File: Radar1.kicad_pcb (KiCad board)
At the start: 4 copper layers, 60 x 42 mm, 99 parts, among them J1 USB4215-03-A, J2 Barrel_Jack, J3 SMA-2.92mm-EndLaunch, J4 SMA-2.92mm-EndLaunch, U1 BGT24LTR11N16, U10 93LC56B-I/SN, U11 445I23D12M00000, U12 AMM-8211PSM, U13 TPS7A4700RGWT, U14 TPS7A2033PDBVR, U15 TPD2E009DBZR, U16 REF5025AID, U2 ADF4159WCCPZ, U3 OPA1656ID, U4 TPS7A2033PDBVR, U5 TPS7A2018PDBVR, U6 TPS7A4700RGWT, U7 FT2232HL-REEL, U8 ADS8353IPW, U9 ADP5600ACPZ-R7, Y1 ECS-TXO-2520MV-500-AN-TR

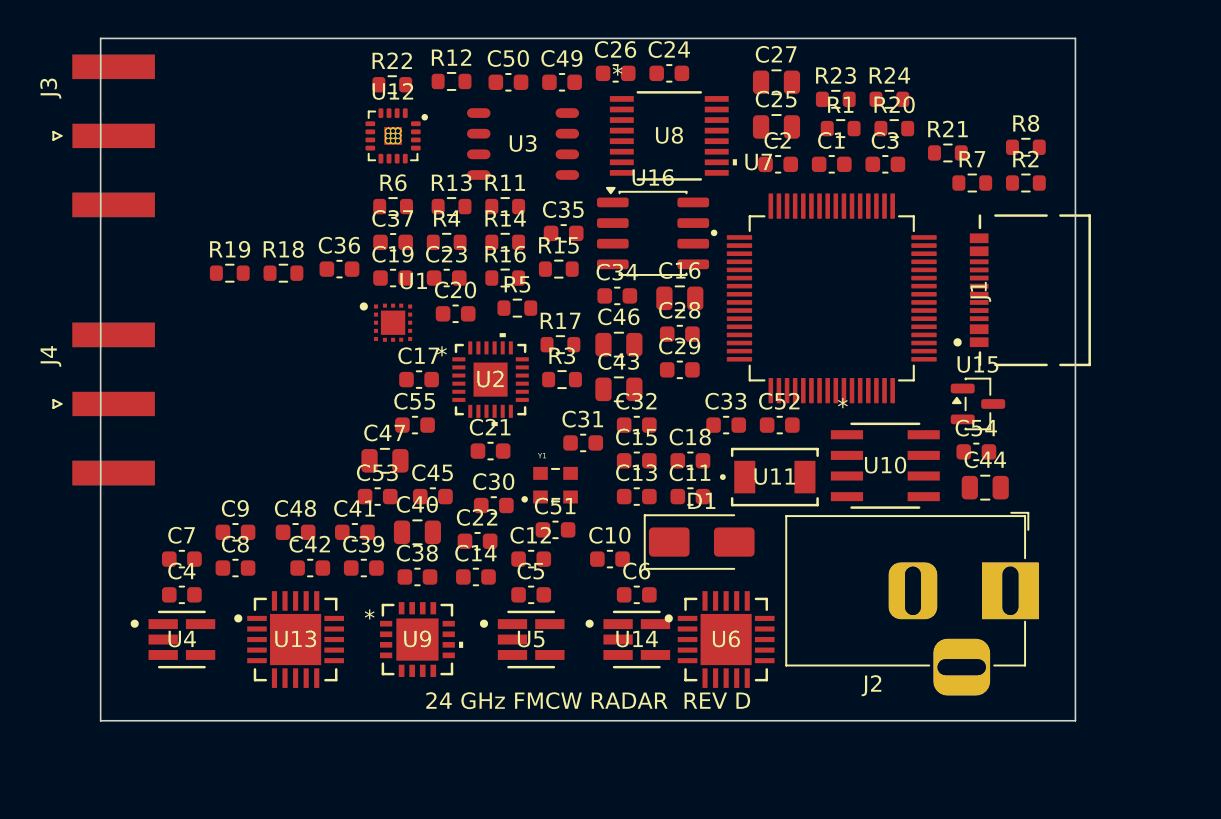
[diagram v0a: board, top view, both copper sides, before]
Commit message: RF routing: GCPW TX/RX lines, 4-layer GND/PWR zones, EP thermal vias
- tools/route_pcb.py (pcbnew API): F.Cu/In1/B.Cu GND zones + In2 +5V zone,
  EP thermal via arrays, 24 GHz GCPW (0.5 mm / 0.25 gap) with GND via fences
- Neck-down to pad width at QFN pad exits (0.5 mm line vs 0.5 mm-pitch pads)
- Via fence self-avoidance against RF copper; RF corridor keepouts in board_gen
  so auto-slotted passives stay out of the GCPW paths
- AMM-8211 footprint: EP thermal vias 9@0.3mm -> 4@0.6mm pitch (fab-safe webs)
- DRC: copper clean; remaining = 172 unconnected (signals, next phase),
  10 J3/J4 edge-launch waivers, silk cosmetics

Co-Authored-By: Claude Fable 5 <noreply@anthropic.com>
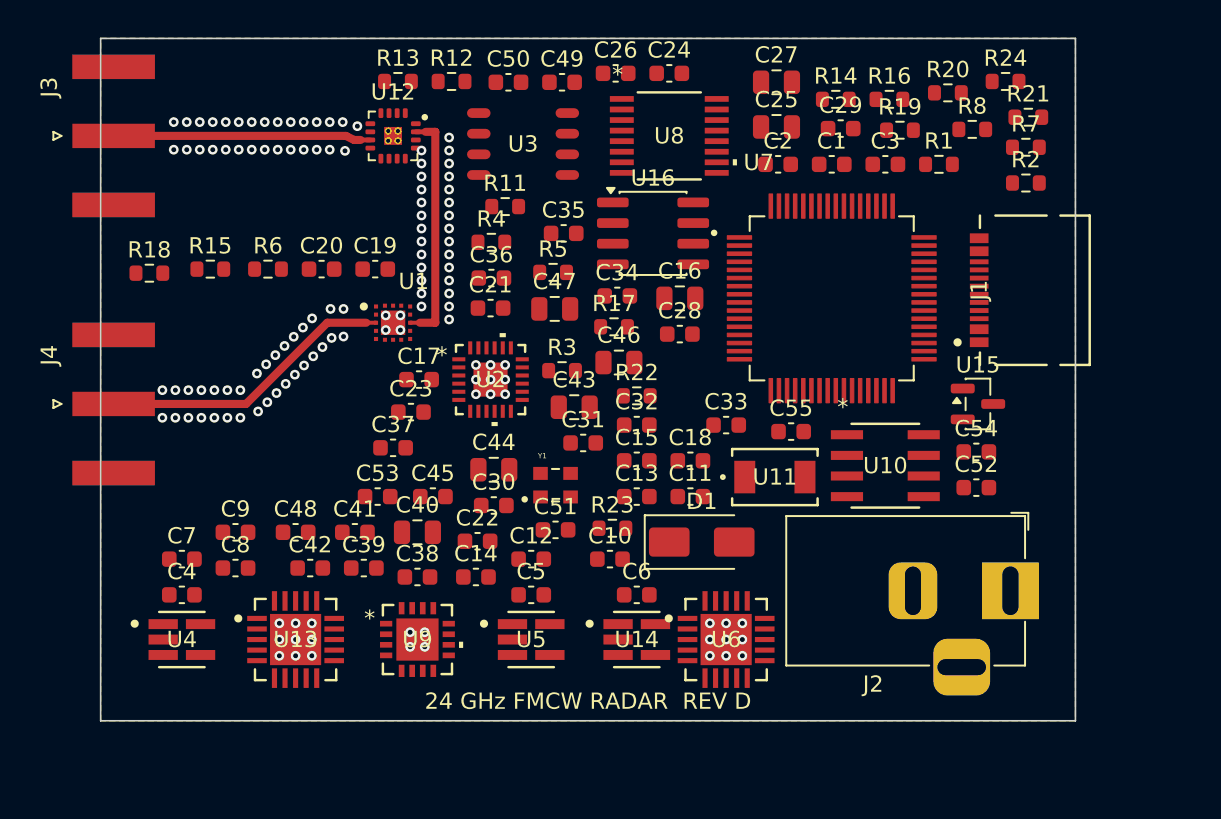
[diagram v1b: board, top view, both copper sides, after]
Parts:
- moved R19 42.2 mm to (109.2, 45.6)
- moved C44 30.3 mm to (84.2, 66.5)
- moved R23 29.8 mm to (91.5, 70.2)
- moved R16 26.1 mm to (108.5, 43.8)
- moved R22 24.4 mm to (93.0, 62.0)
- moved C55 23.2 mm to (102.5, 64.2)
- moved R14 22.2 mm to (105.2, 43.8)
- moved R15 21.5 mm to (66.8, 54.2)
- moved C29 17.8 mm to (105.5, 45.5)
- moved C47 14.0 mm to (88.0, 56.6)
- moved C52 12.7 mm to (113.9, 67.7)
- moved C37 12.7 mm to (78.0, 65.2)
- moved C36 9.37 mm to (84.0, 54.8)
- moved C21 8.80 mm to (84.0, 56.6)
- moved C20 8.70 mm to (73.6, 54.2)
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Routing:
- net ANT_RX: track 0.00 -> 18.2 mm
- net ANT_TX: track 0.00 -> 15.9 mm
- net RF_TX: track 0.00 -> 14.5 mm
- net GND: vias 0 -> 125
- added copper zone on In2.Cu, net +5V
- added copper zone on B.Cu, net GND
- added copper zone on F.Cu, net GND
- added copper zone on In1.Cu, net GND

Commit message: Phase C routing: A* signal/power router, In2 split planes, board 66x46
tools/route_signals.py: 0.2mm-grid A* over F.Cu/B.Cu with through-vias.
- escape stubs on fine-pitch ICs, escape-limited nets routed first
- In2 becomes a split plane: +3V3_RF west / +1V8 center / +3V3_DIG east
  over the +5V base fill; rail pads stitch down with vias, stragglers
  routed as tracks; GND stitching to In1 near every ground pad
- rip-up & reroute for sealed legs; geometric heal pass reconnects
  cluster splits from exact copper geometry
- board grown 60x42 -> 66x46 (placement was at ~95% usable density),
  edge connectors and south LDO row shifted with the edges
- board_gen: courtyard-based bboxes, RF-pocket ownership guard, IC
  routing halos, U2/U7 bus-lane keepouts, stair-stepped ANT_RX keepout

DRC: 172 -> 28 unconnected items (19 net splits remain, all in the RF
pocket / U2-east / U7-west / J1 congestion spots); zero clearance or
short errors; 10 J3/J4 edge-launch waivers as before. Renders in docs/.

Co-Authored-By: Claude Fable 5 <noreply@anthropic.com>
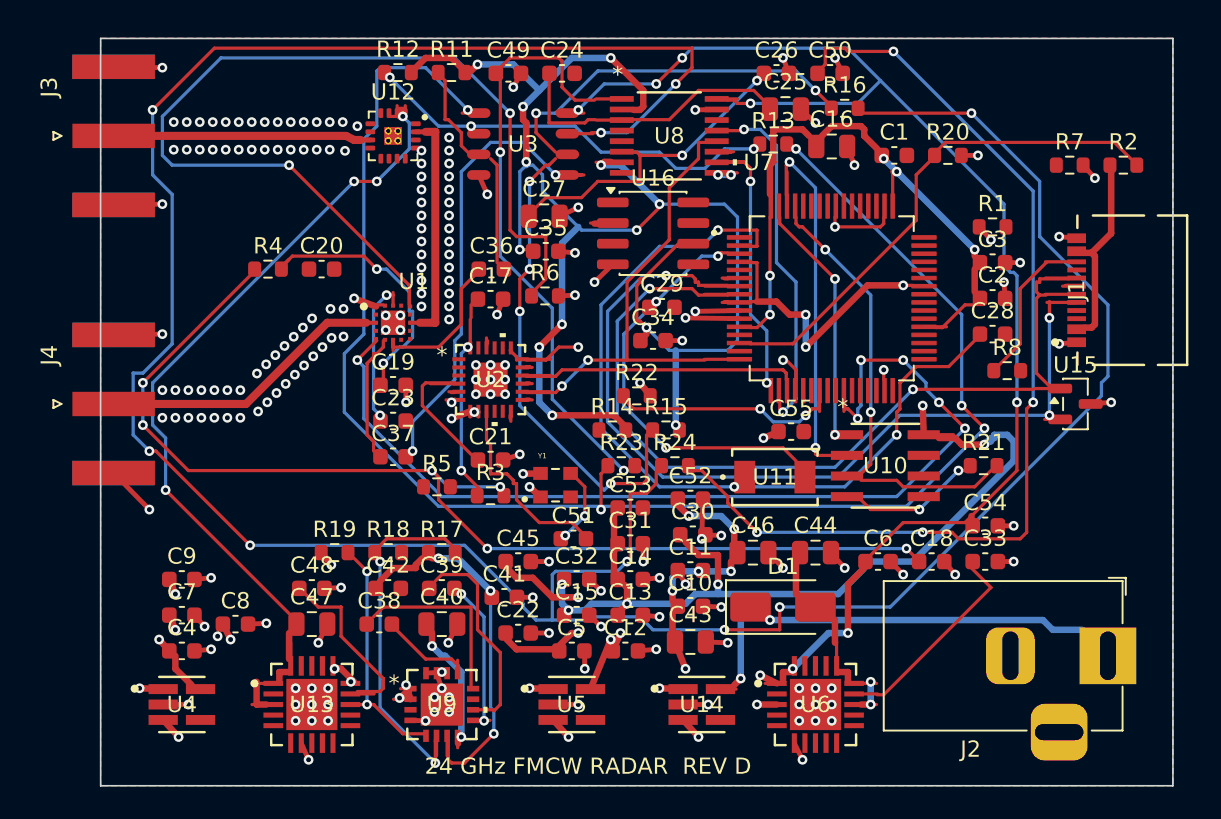
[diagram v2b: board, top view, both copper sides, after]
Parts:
- moved R19 43.4 mm to (74.4, 71.7)
- moved R24 31.2 mm to (95.3, 66.3)
- moved R15 29.7 mm to (94.8, 64.1)
- moved R14 24.6 mm to (91.5, 64.1)
- moved C47 24.5 mm to (73.0, 76.0)
- moved R13 23.4 mm to (101.4, 46.5)
- moved R18 22.6 mm to (77.7, 71.7)
- moved R21 21.6 mm to (114.3, 66.3)
- moved C44 20.4 mm to (104.0, 71.7)
- moved C50 19.8 mm to (104.9, 42.1)
- moved C28 19.2 mm to (114.9, 58.2)
- moved C33 18.0 mm to (114.5, 72.2)
- moved C52 17.6 mm to (96.3, 68.3)
- moved R17 17.5 mm to (81.0, 71.7)
- moved R6 17.1 mm to (87.3, 55.9)
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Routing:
- net IFB_OUT: track 0.00 -> 181.3 mm, vias 0 -> 9
- net +5V: track 0.00 -> 122.8 mm, vias 0 -> 25
- net IFA_OUT: track 0.00 -> 98.3 mm, vias 0 -> 5
- net VREF: track 0.00 -> 95.5 mm, vias 0 -> 13
- net GND: track 0.00 -> 85.7 mm, vias 125 -> 190
- net +3V3_DIG: track 0.00 -> 83.2 mm, vias 0 -> 12
- net LF_B: track 0.00 -> 68.3 mm, vias 0 -> 6
- net ADC_B: track 0.00 -> 61.8 mm, vias 0 -> 4
- net BGT_TXEN: track 0.00 -> 61.0 mm, vias 0 -> 6
- net USB_DP: track 0.00 -> 59.7 mm, vias 0 -> 2
- net RTUNE_N: track 0.00 -> 59.4 mm, vias 0 -> 2
- net USB_DM: track 0.00 -> 58.8 mm, vias 0 -> 3
- net +3V0_PA: track 0.00 -> 52.6 mm, vias 0 -> 4
- net IFB_INV: track 0.00 -> 52.0 mm, vias 0 -> 6
- net OSC_I: track 0.00 -> 51.2 mm, vias 0 -> 3
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- added copper zone on In2.Cu, net +1V8
- added copper zone on In2.Cu, net +3V3_DIG
- added copper zone on In2.Cu, net +3V3_RF
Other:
- board size 60 x 42 mm -> 66 x 46 mm

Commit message: Routing: thin-width heal class (0.15mm), regenerate at best config
DRC: 28 unconnected items (18 net splits) remain, concentrated at the
RF-pocket wall crossings (-VGG, DIVO, LF_C, +3V3_RF at U1/U12), the U2
east SPI column, U7 west, and J1. Copper otherwise clean: no clearance,
short, or hole errors; 10 J3/J4 edge-launch waivers by design.
Next: hand-finish the last splits (probe-driven, or KiCad GUI).

Co-Authored-By: Claude Fable 5 <noreply@anthropic.com>
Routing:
- net +3V3_RF: track 15.0 -> 63.8 mm, vias 12 -> 18
- net +5V: track 122.8 -> 127.7 mm, vias 25 -> 24
- net GND: track 85.7 -> 82.6 mm, vias 190 -> 187
- net VGG_CP: track 8.40 -> 10.6 mm
- net +3V3_DIG: track 83.2 -> 82.1 mm
- net IFA_OUT: track 98.3 -> 97.2 mm
- net BGT_TXEN: track 61.0 -> 60.0 mm
- net ADF_REFIN: track 11.6 -> 12.5 mm
- net +1V8: track 26.5 -> 25.9 mm, vias 10 -> 9
- net LF_C: track 15.4 -> 16.0 mm
- net U9C2N: track 9.42 -> 8.90 mm
- net USB_RESET: track 29.7 -> 30.1 mm, vias 0 -> 2
- net ADC_B: track 61.8 -> 62.2 mm, vias 4 -> 2
- net IFB_OUT: vias 9 -> 13

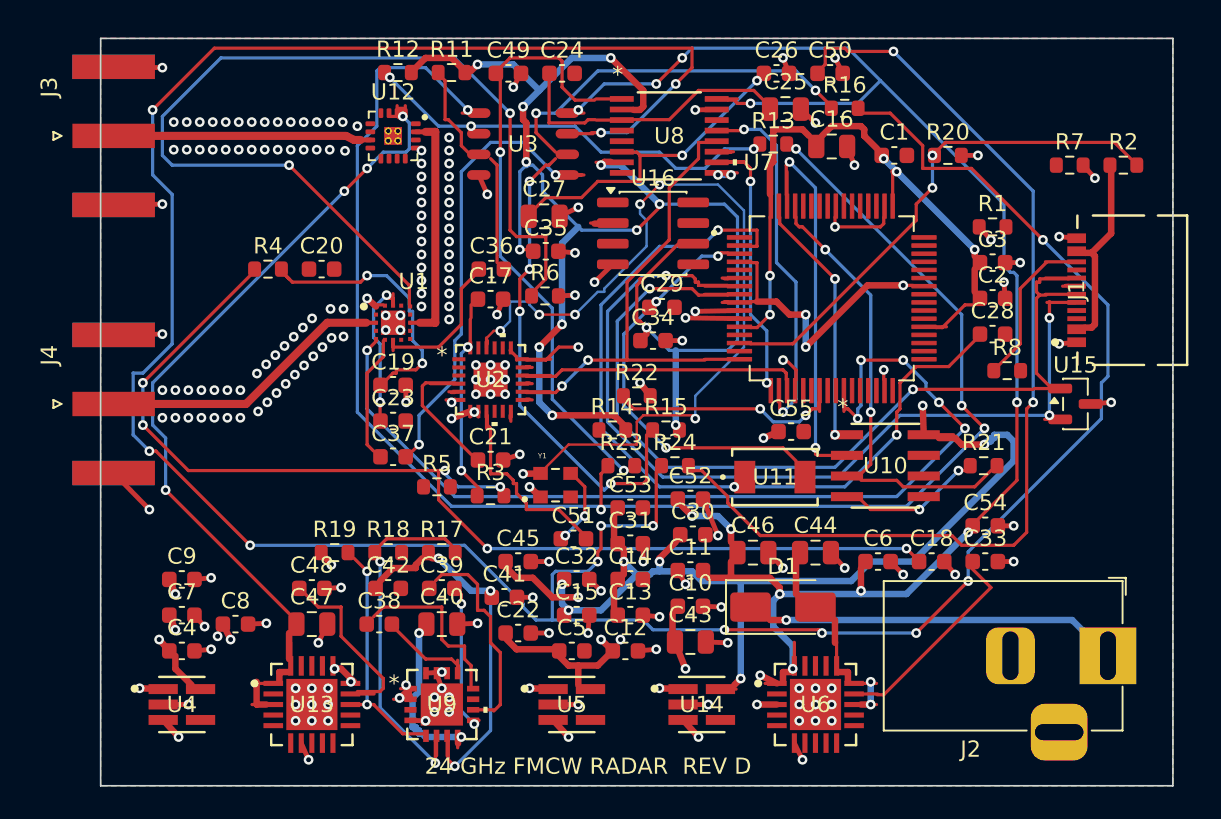
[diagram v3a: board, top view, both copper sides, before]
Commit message: Finisher pass 1: exact via-feasibility map, GND re-stitch; 28 -> 25 unconnected
Co-Authored-By: Claude Fable 5 <noreply@anthropic.com>
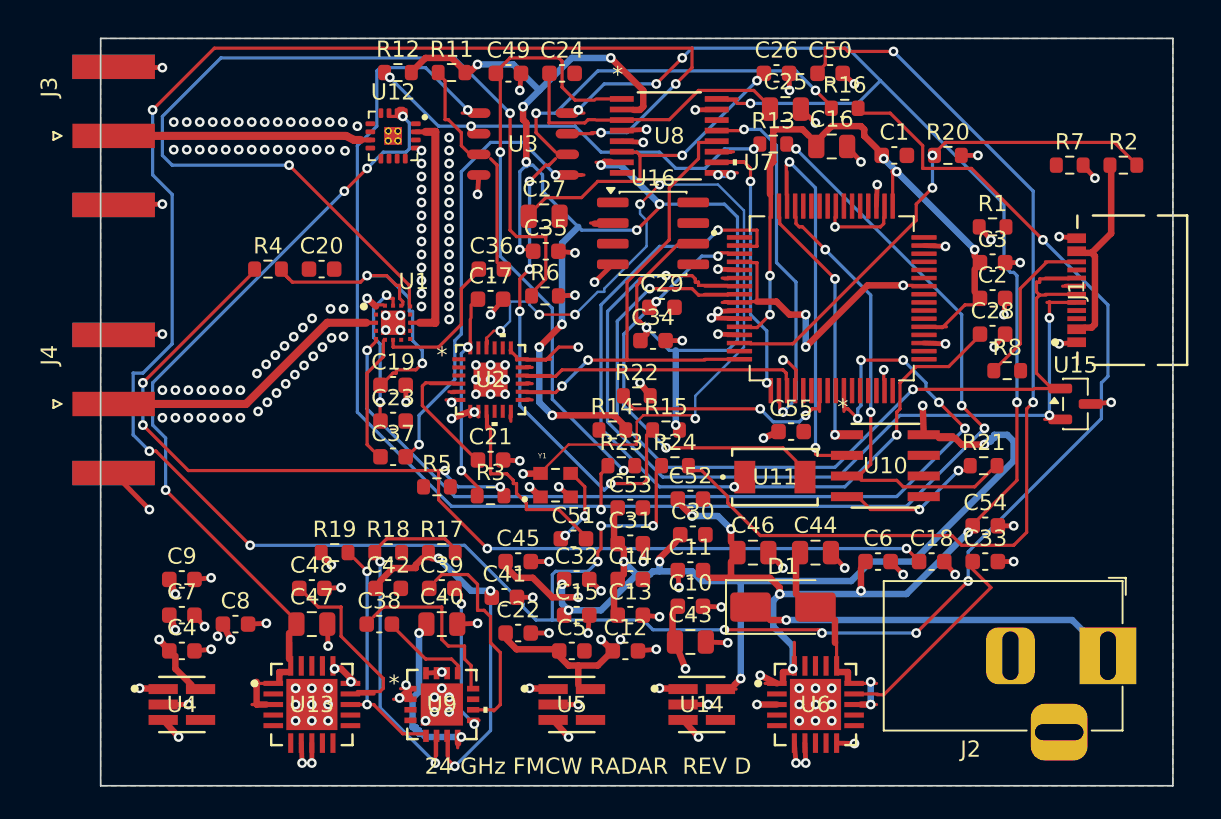
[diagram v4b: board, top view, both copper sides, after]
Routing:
- net GND: track 82.6 -> 89.5 mm, vias 187 -> 197
- net LF_C: track 16.0 -> 19.5 mm
- net +3V0_PA: track 52.6 -> 51.7 mm
- net U9C1N: track 5.71 -> 4.91 mm
- net VPTAT_N: track 9.52 -> 8.78 mm
- net IFI_IN: track 9.18 -> 8.51 mm

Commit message: Finisher: transactional rip-heal, corner-safe pad model; 25 -> 23 unconnected
Co-Authored-By: Claude Fable 5 <noreply@anthropic.com>
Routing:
- net ADF_CE: track 0.81 -> 110.4 mm, vias 0 -> 14
- net +5V: track 127.7 -> 179.3 mm, vias 24 -> 35
- net Net-(U7-REF): track 1.26 -> 45.1 mm, vias 0 -> 6
- net -VGG: track 22.4 -> 64.7 mm, vias 3 -> 9
- net IFB_INV: track 52.0 -> 80.3 mm, vias 6 -> 8
- net U9C2N: track 8.90 -> 30.5 mm, vias 2 -> 3
- net GND: track 89.5 -> 70.5 mm, vias 197 -> 181
- net CC1_N: track 0.00 -> 16.4 mm, vias 0 -> 4
- net RSET_N: track 0.00 -> 16.0 mm, vias 0 -> 4
- net ADC_B: track 62.2 -> 76.5 mm, vias 2 -> 4
- net IFB_INP: track 27.0 -> 38.1 mm, vias 2 -> 4
- net ADC_A: track 37.2 -> 27.4 mm, vias 2 -> 4
- net EE_DATA: track 26.7 -> 35.2 mm
- net IFA_INP: track 11.9 -> 19.0 mm
- net ADF_MUXOUT: track 15.3 -> 21.7 mm, vias 2 -> 4
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
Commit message: Finisher iteration: 23 -> 22 unconnected; 6 capacity-limited nets remain
Remaining splits: +3V3_RF (U1.9 pocket), ADF_TXDATA, CS_ADC, SPI_MOSI
(U2->U7 SPI corridor at capacity), DIVO (U1 south escape slot), RFINA_N
(pocket wall). These need a placement nudge or GUI routing; every
rip/swap transaction rolls back because the corridors are full.

Co-Authored-By: Claude Fable 5 <noreply@anthropic.com>
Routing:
- net ADC_A: track 27.4 -> 39.1 mm
